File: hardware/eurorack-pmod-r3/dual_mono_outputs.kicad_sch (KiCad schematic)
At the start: 18 parts, among them J10 PJ398SM, J9 PJ398SM, U6 TL074, U7 TL074

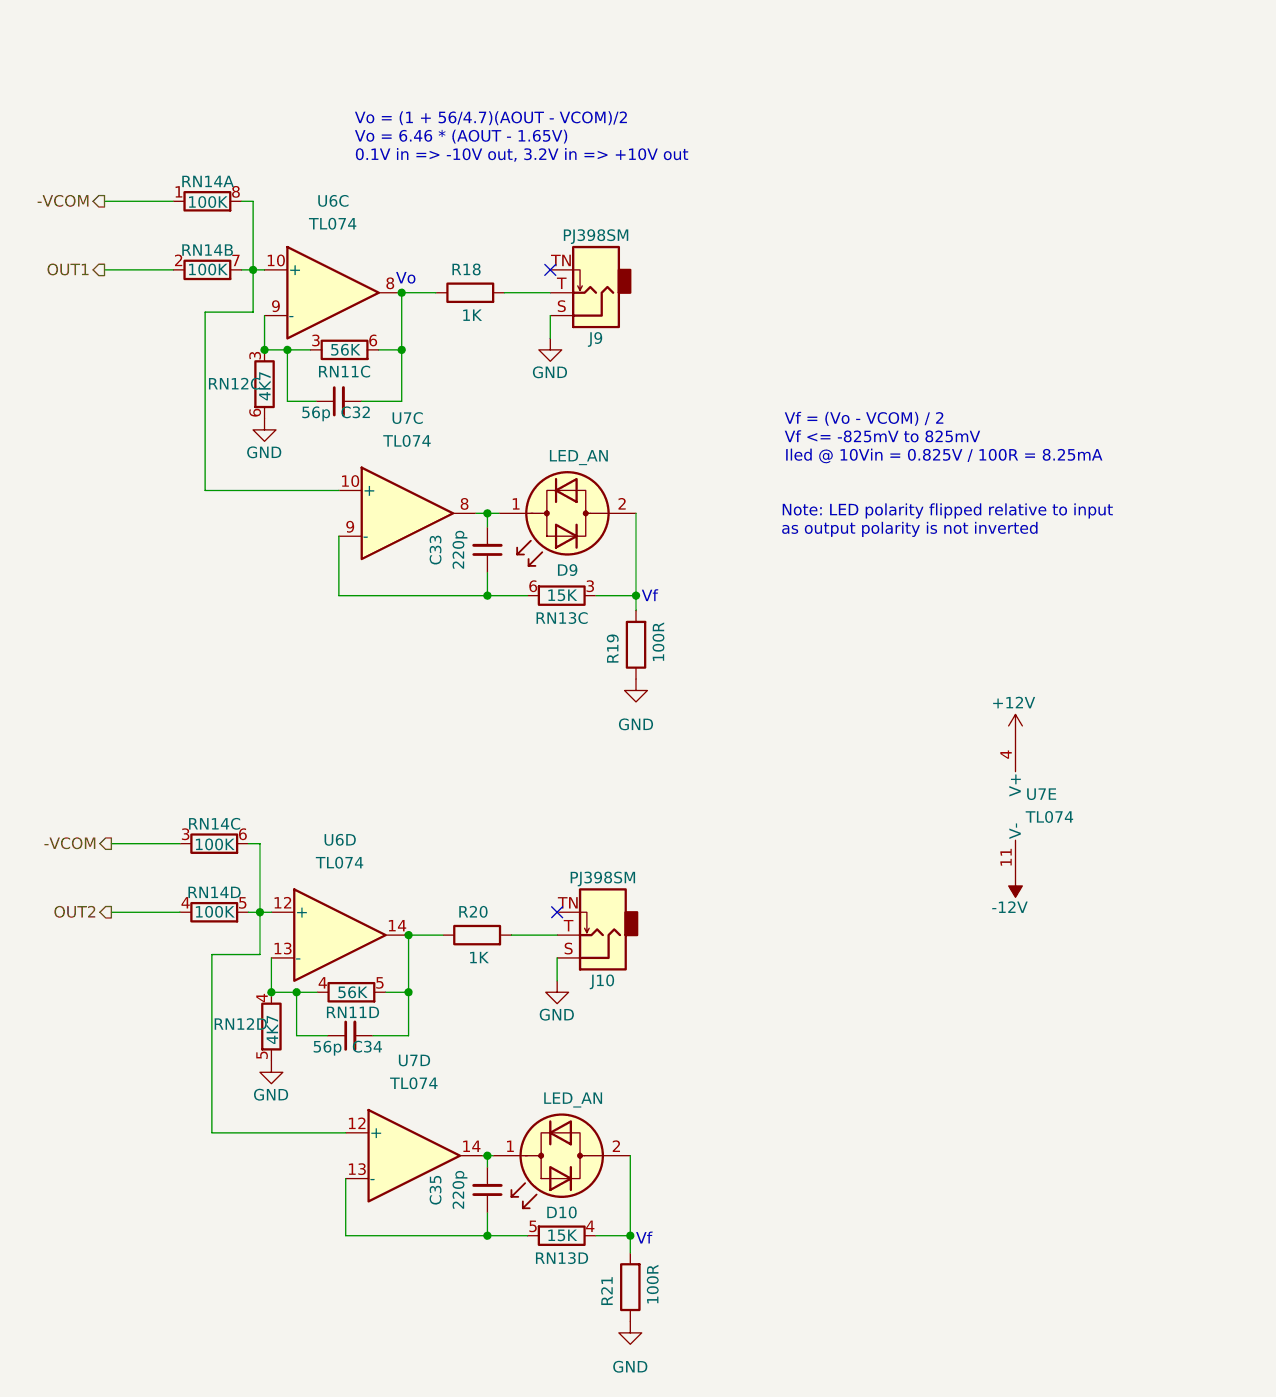
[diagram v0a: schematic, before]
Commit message: rev3: try positioning new jacks
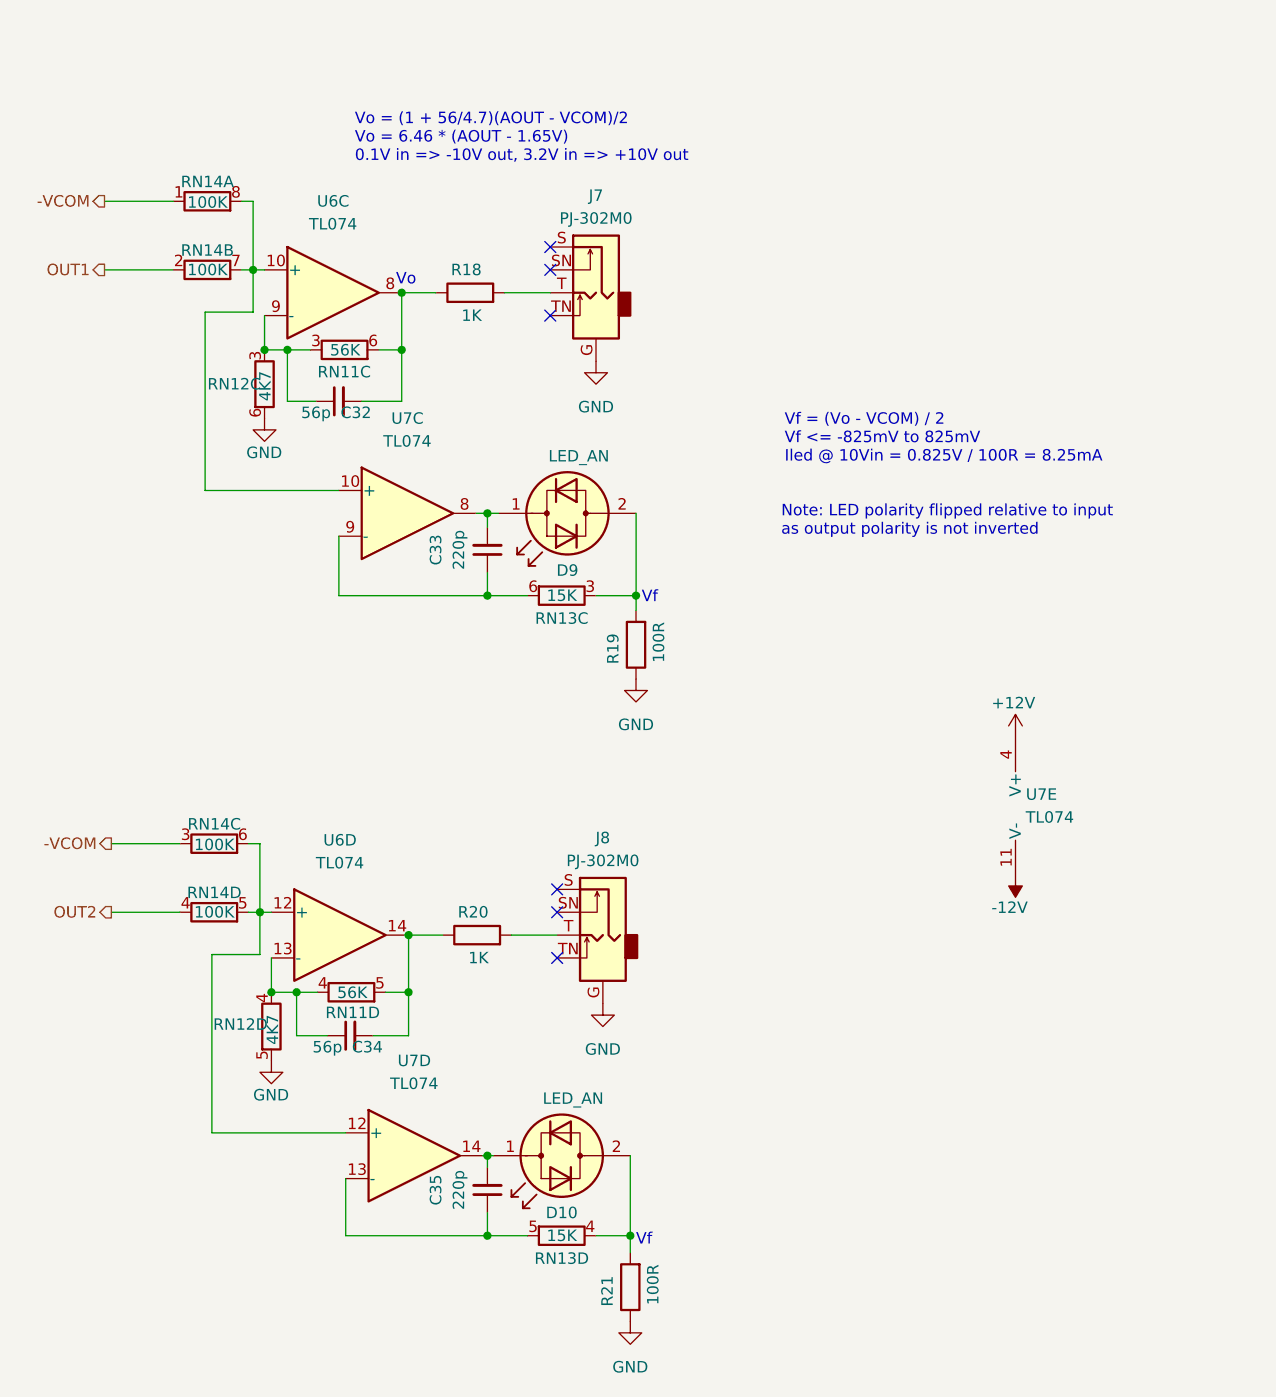
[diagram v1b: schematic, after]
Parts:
- removed J10, J9: PJ398SM, AudioJacks:Jack_3.5mm_QingPu_WQP-PJ302M_Horizontal, symbol Connector:AudioJack2_SwitchT
- added J7, J8: PJ-302M0, AudioJacksFixed:pj324m, symbol Connector:AudioJack2_Ground_Switch
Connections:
- net GND: now also J7.G, J8.G
- net at R20.2: now also J8.T
- net at R18.2: now also J7.T
- no-connect marks 2 -> 6
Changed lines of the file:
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@@
   (junction (at 66.675 70.231) (diameter 0) (color 0 0 0 0)
   )
+  (no_connect (at 73.66 48.26))
+  (no_connect (at 73.66 40.64))
   (no_connect (at 73.66 43.18))
   (no_connect (at 74.422 114.554))
+  (no_connect (at 74.422 119.634))
+  (no_connect (at 74.422 112.014))
   (wire (pts (xy 42.672 123.444) (xy 42.672 119.634))
     (stroke (width 0) (type default) (color 0 0 0 0))
@@
     (stroke (width 0) (type default) (color 0 0 0 0))
   )
-  (wire (pts (xy 73.66 48.26) (xy 73.66 50.8))
-    (stroke (width 0) (type default) (color 0 0 0 0))
-  )
   (wire (pts (xy 69.342 117.094) (xy 74.422 117.094))
     (stroke (width 0) (type default) (color 0 0 0 0))
@@
   )
   (wire (pts (xy 66.675 70.231) (xy 66.675 71.755))
-    (stroke (width 0) (type default) (color 0 0 0 0))
-  )
-  (wire (pts (xy 74.422 119.634) (xy 74.422 122.174))
     (stroke (width 0) (type default) (color 0 0 0 0))
   )
@@
     (pin "1")
   )
-  (symbol (lib_id "Connector:AudioJack2_SwitchT") (at 79.502 117.094 180) (unit 1)
-    (in_bom yes) (on_board yes)
-    (property "Reference" "J10" (id 0) (at 79.502 122.174 0))
-    (property "Value" "PJ398SM" (id 1) (at 79.502 110.744 0))
-    (property "Footprint" "AudioJacks:Jack_3.5mm_QingPu_WQP-PJ302M_Horizontal" (id 2) (at 79.502 117.094 0)
-      (effects (font (size 1.27 1.27)) hide)
-    )
-    (property "Datasheet" "" (id 3) (at 79.502 117.094 0)
-      (effects (font (size 1.27 1.27)) hide)
-    )
-    (pin "S")
-    (pin "T")
-    (pin "TN")
-  )
   (symbol (lib_id "power:+12V") (at 125.349 95.123 0) (unit 1)
     (in_bom yes) (on_board yes)
@@
     )
     (property "Datasheet" "" (id 3) (at 125.349 95.123 0)
+      (effects (font (size 1.27 1.27)) hide)
+    )
+    (pin "1")
+  )
+  (symbol (lib_id "power:GND") (at 79.502 124.714 0) (mirror y) (unit 1)
+    (in_bom yes) (on_board yes) (fields_autoplaced)
+    (property "Reference" "#PWR059" (id 0) (at 79.502 131.064 0)
+      (effects (font (size 1.27 1.27)) hide)
+    )
+    (property "Value" "GND" (id 1) (at 79.502 129.794 0))
+    (property "Footprint" "" (id 2) (at 79.502 124.714 0)
+      (effects (font (size 1.27 1.27)) hide)
+    )
+    (property "Datasheet" "" (id 3) (at 79.502 124.714 0)
       (effects (font (size 1.27 1.27)) hide)
     )
@@
     (pin "4")
   )
-  (symbol (lib_id "power:GND") (at 74.422 122.174 0) (unit 1)
-    (in_bom yes) (on_board yes)
-    (property "Reference" "#PWR082" (id 0) (at 74.422 128.524 0)
-      (effects (font (size 1.27 1.27)) hide)
-    )
-    (property "Value" "GND" (id 1) (at 72.39 125.984 0)
-      (effects (font (size 1.27 1.27)) (justify left))
-    )
-    (property "Footprint" "" (id 2) (at 74.422 122.174 0)
-      (effects (font (size 1.27 1.27)) hide)
-    )
-    (property "Datasheet" "" (id 3) (at 74.422 122.174 0)
-      (effects (font (size 1.27 1.27)) hide)
-    )
-    (pin "1")
-  )
   (symbol (lib_id "Device:C_Small") (at 66.675 145.415 180) (unit 1)
     (in_bom yes) (on_board yes)
@@
     (pin "1")
   )
+  (symbol (lib_id "Connector:AudioJack2_Ground_Switch") (at 78.74 45.72 0) (mirror y) (unit 1)
+    (in_bom yes) (on_board yes)
+    (property "Reference" "J7" (id 0) (at 78.74 34.925 0))
+    (property "Value" "PJ-302M0" (id 1) (at 78.74 37.465 0))
+    (property "Footprint" "AudioJacksFixed:pj324m" (id 2) (at 78.74 40.64 0)
+      (effects (font (size 1.27 1.27)) hide)
+    )
+    (property "Datasheet" "~" (id 3) (at 78.74 40.64 0)
+      (effects (font (size 1.27 1.27)) hide)
+    )
+    (pin "G")
+    (pin "S")
+    (pin "SN")
+    (pin "T")
+    (pin "TN")
+  )
   (symbol (lib_id "power:-12V") (at 125.349 110.363 180) (unit 1)
     (in_bom yes) (on_board yes)
@@
     )
     (pin "1")
+  )
+  (symbol (lib_id "Connector:AudioJack2_Ground_Switch") (at 79.502 117.094 0) (mirror y) (unit 1)
+    (in_bom yes) (on_board yes)
+    (property "Reference" "J8" (id 0) (at 79.502 106.299 0))
+    (property "Value" "PJ-302M0" (id 1) (at 79.502 108.839 0))
+    (property "Footprint" "AudioJacksFixed:pj324m" (id 2) (at 79.502 112.014 0)
+      (effects (font (size 1.27 1.27)) hide)
+    )
+    (property "Datasheet" "~" (id 3) (at 79.502 112.014 0)
+      (effects (font (size 1.27 1.27)) hide)
+    )
+    (pin "G")
+    (pin "S")
+    (pin "SN")
+    (pin "T")
+    (pin "TN")
   )
   (symbol (lib_id "Device:R_Pack04_Split") (at 42.672 127.254 180) (unit 4)
@@
     (pin "5")
   )
-  (symbol (lib_id "Connector:AudioJack2_SwitchT") (at 78.74 45.72 180) (unit 1)
-    (in_bom yes) (on_board yes)
-    (property "Reference" "J9" (id 0) (at 78.74 50.8 0))
-    (property "Value" "PJ398SM" (id 1) (at 78.74 39.37 0))
-    (property "Footprint" "AudioJacks:Jack_3.5mm_QingPu_WQP-PJ302M_Horizontal" (id 2) (at 78.74 45.72 0)
-      (effects (font (size 1.27 1.27)) hide)
-    )
-    (property "Datasheet" "" (id 3) (at 78.74 45.72 0)
-      (effects (font (size 1.27 1.27)) hide)
-    )
-    (pin "S")
-    (pin "T")
-    (pin "TN")
+  (symbol (lib_id "power:GND") (at 78.74 53.34 0) (mirror y) (unit 1)
+    (in_bom yes) (on_board yes) (fields_autoplaced)
+    (property "Reference" "#PWR056" (id 0) (at 78.74 59.69 0)
+      (effects (font (size 1.27 1.27)) hide)
+    )
+    (property "Value" "GND" (id 1) (at 78.74 58.42 0))
+    (property "Footprint" "" (id 2) (at 78.74 53.34 0)
+      (effects (font (size 1.27 1.27)) hide)
+    )
+    (property "Datasheet" "" (id 3) (at 78.74 53.34 0)
+      (effects (font (size 1.27 1.27)) hide)
+    )
+    (pin "1")
   )
   (symbol (lib_id "Device:R_Pack04_Split") (at 51.562 123.444 270) (unit 4)
@@
     (pin "5")
   )
-  (symbol (lib_id "power:GND") (at 73.66 50.8 0) (unit 1)
-    (in_bom yes) (on_board yes)
-    (property "Reference" "#PWR077" (id 0) (at 73.66 57.15 0)
-      (effects (font (size 1.27 1.27)) hide)
-    )
-    (property "Value" "GND" (id 1) (at 71.628 54.61 0)
-      (effects (font (size 1.27 1.27)) (justify left))
-    )
-    (property "Footprint" "" (id 2) (at 73.66 50.8 0)
-      (effects (font (size 1.27 1.27)) hide)
-    )
-    (property "Datasheet" "" (id 3) (at 73.66 50.8 0)
-      (effects (font (size 1.27 1.27)) hide)
-    )
-    (pin "1")
-  )
   (symbol (lib_id "power:GND") (at 42.672 131.064 0) (unit 1)

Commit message: rev3/schematic: cal mem / jack detect / i2c LEDs / power fixes
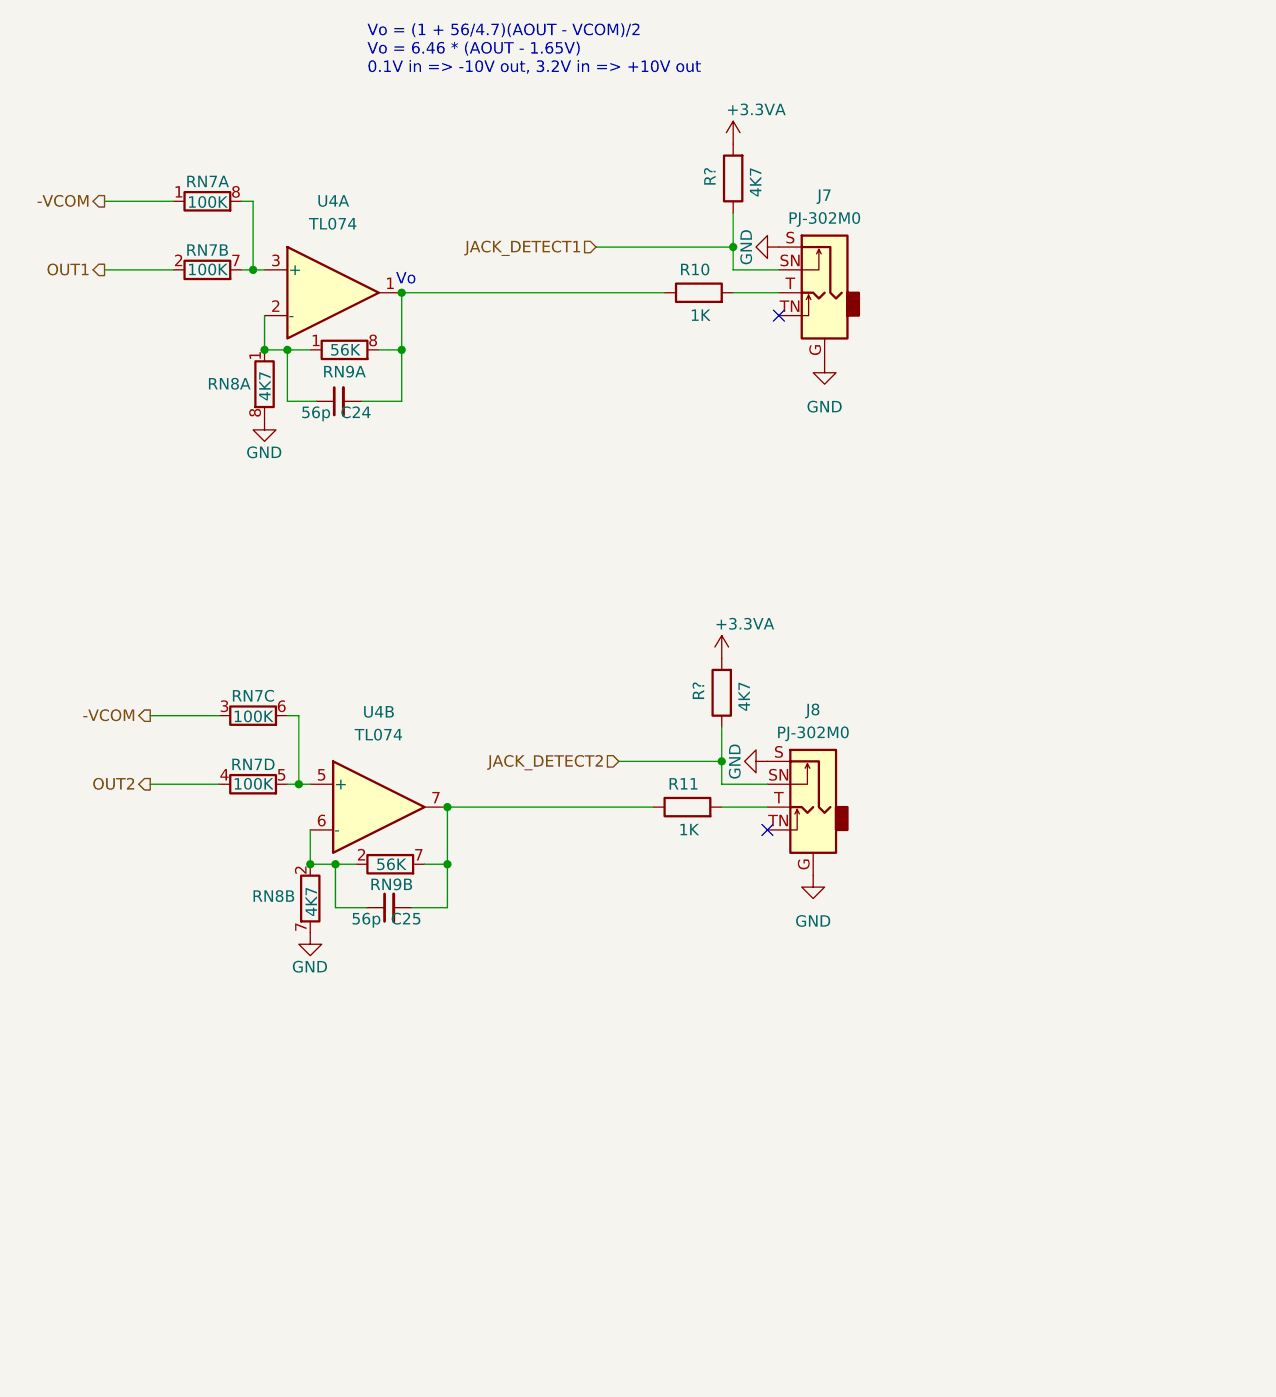
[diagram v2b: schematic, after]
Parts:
- removed C33, C35: 220p, Capacitor_SMD:C_0603_1608Metric, symbol Device:C_Small
- removed D10, D9: LED_AN, LED_SMD:LED_1206_3216Metric, symbol Device:LED_Dual_Bidirectional
- removed R19, R21: 100R, Resistor_SMD:R_0603_1608Metric, symbol Device:R
- removed RN13: 15K, Resistor_SMD:R_Cat16-4, symbol Device:R_Pack04_Split
- removed U7: TL074, Package_SO:TSSOP-14_4.4x5mm_P0.65mm, symbol Amplifier_Operational:TL074
- added R? (x2): 4K7, Resistor_SMD:R_0603_1608Metric, symbol Device:R
- renumbered C32 to C24, C34 to C25, R18 to R10, R20 to R11, RN14 to RN7, RN12 to RN8, RN11 to RN9, U6 to U4
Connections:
- net GND: now also J7.S, J8.S, RN8.7 (R2.2), RN8.8 (R1.2); no longer RN8.5 (R4.2), RN8.6 (R3.2)
- net at RN7.5 (R4.2), RN7.6 (R3.2): now also U4.5 (+); no longer U4.12 (+)
- net at RN7.7 (R2.2), RN7.8 (R1.2): now also U4.3 (+); no longer U4.10 (+)
- net at C24.2, R10.1: now also RN9.8 (R1.2), U4.1; no longer RN9.6 (R3.2), U4.8
- net JACK_DETECT1: now reaches J7.SN
- net JACK_DETECT1: now also R?.1
- net JACK_DETECT2: now reaches J8.SN
- net JACK_DETECT2: now also R?.1
- net at C25.2, R11.1: now also RN9.7 (R2.2), U4.7; no longer RN9.5 (R4.2), U4.14
- new net: C24.1, RN8.1 (R1.1), RN9.1 (R1.1), U4.2 (-)
- new net: C25.1, RN8.2 (R2.1), RN9.2 (R2.1), U4.6 (-)
- new net +3.3VA: R?.2, R?.2
- no-connect marks 6 -> 2
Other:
- note removed: "Note: LED polarity flipped relative to input as output polarity is not inverted"
- note removed: "Vf"
- note removed: "Vf = (Vo - VCOM) / 2 Vf <= -825mV to 825mV Iled @ 10Vin = 0.825V / 100R = 8.25mA"
- moved on the sheet: C25, J7, J8, R10, R11, RN7C, RN7D, RN8B, RN9B, U4B
